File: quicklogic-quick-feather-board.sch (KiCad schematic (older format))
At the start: 48 parts, among them IC1 EOS-S3, J5 0473460001, Q1 BSS138AKA, Q2 BSS84, U1 TPS62821DLCR, U2 MCP73831T-2ACI_OT, U3 GD25Q16CWIGR, U4 DPS310, U5 MC3635, X1 ECS-_327-12_5-34B-TR

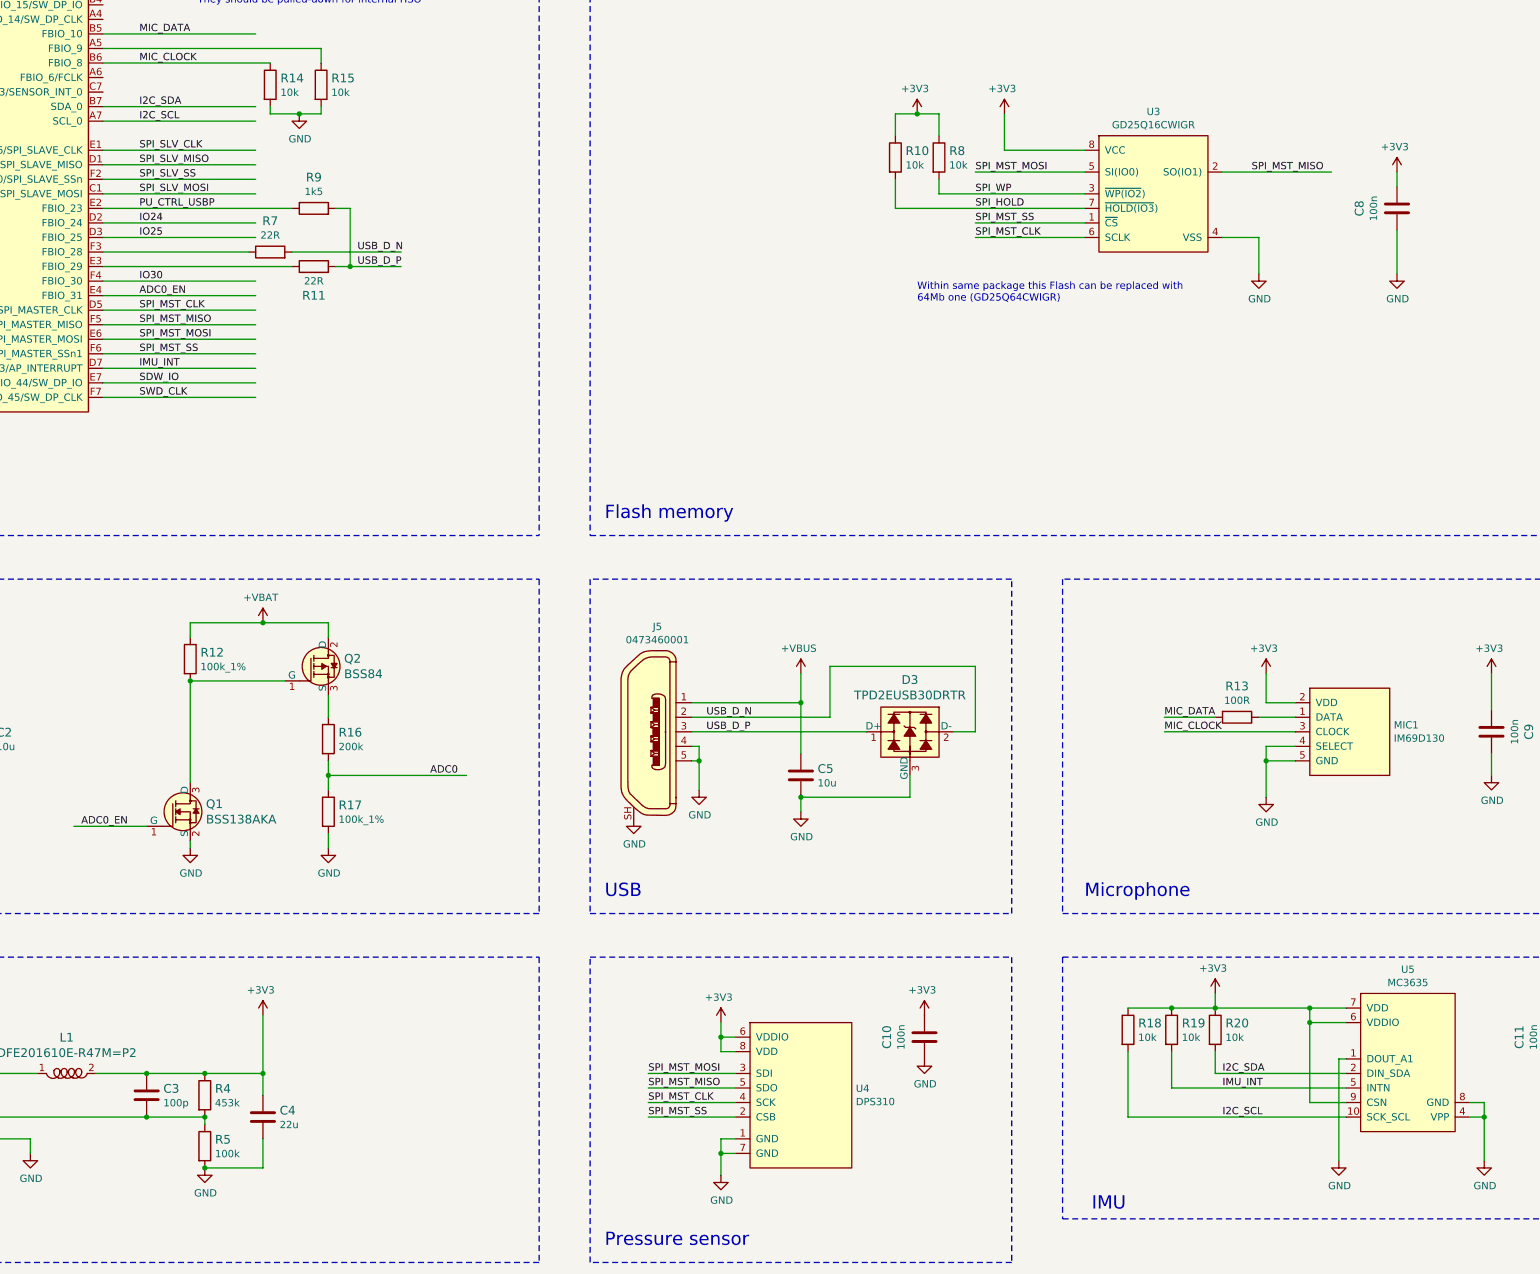
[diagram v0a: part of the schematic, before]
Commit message: Added bootstrap resistors, connected pressure sensor to I2C bus, placed components on PCB
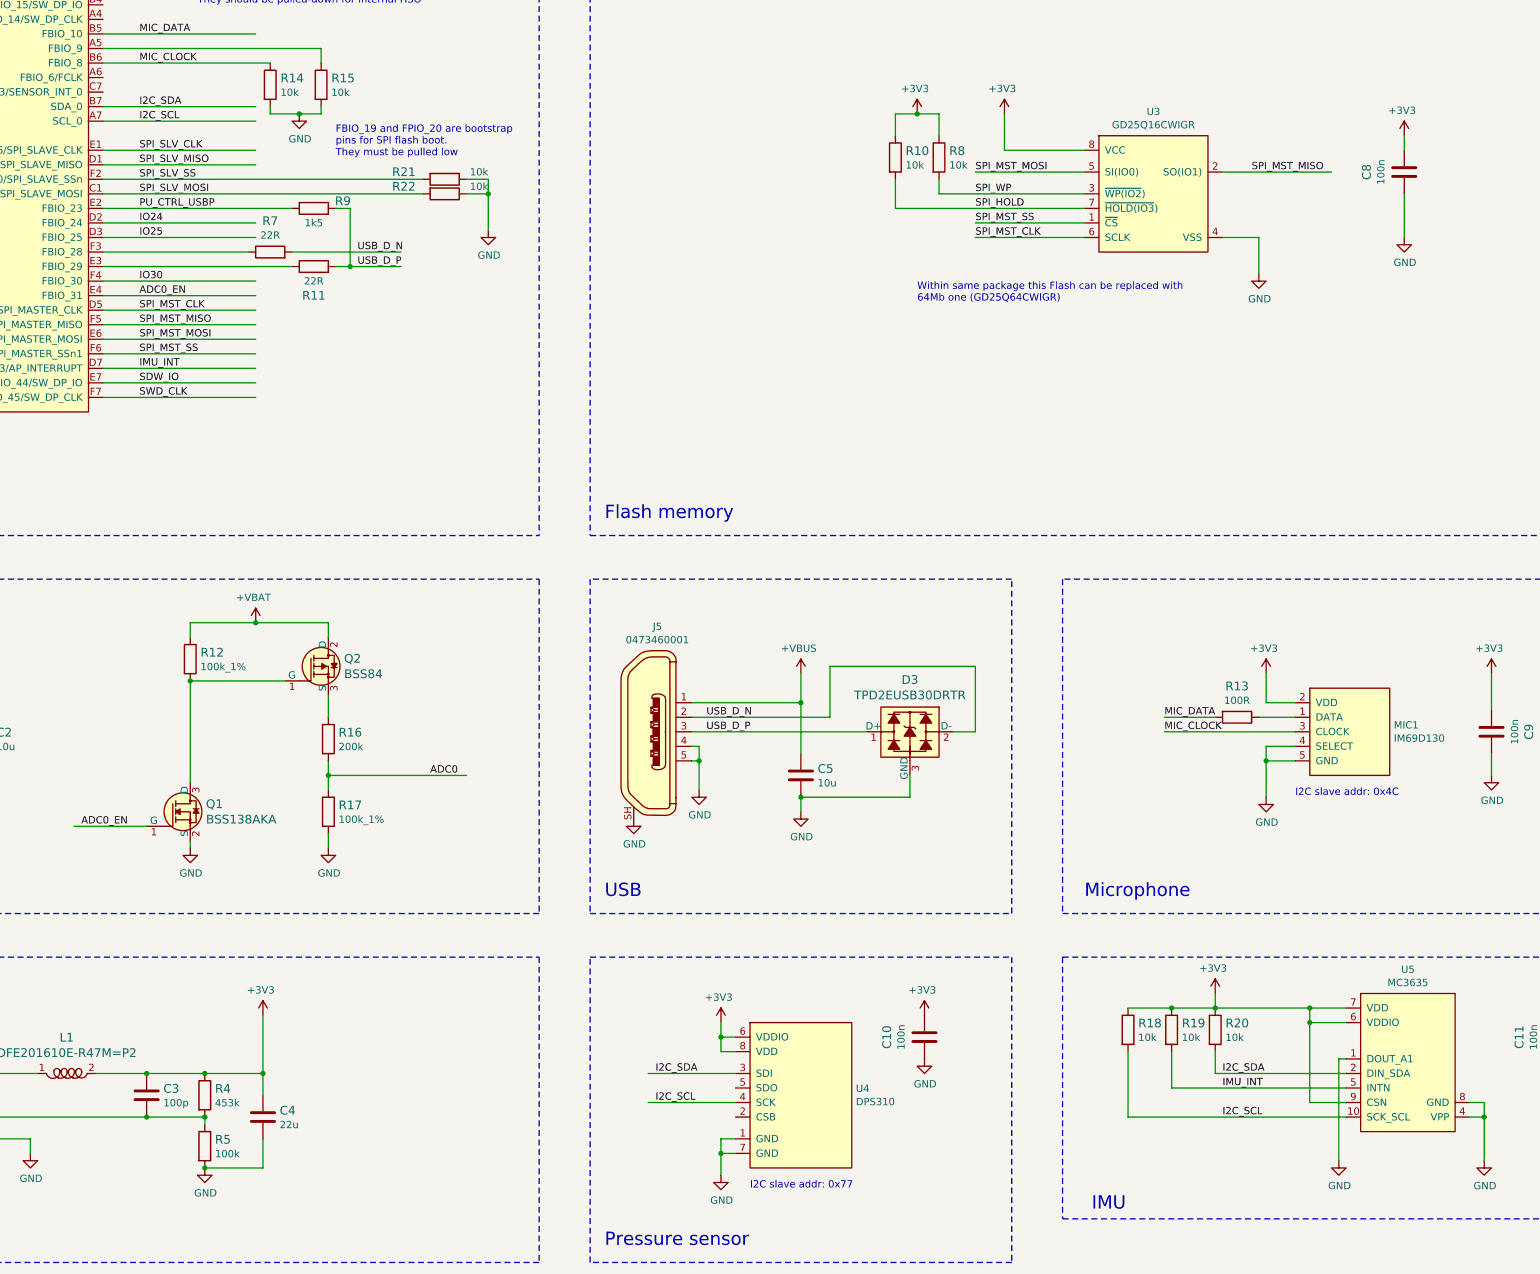
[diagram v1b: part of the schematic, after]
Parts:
- added R21, R22: R_10k_0402, quicklogic-quick-feather-board-footprints:0402-res, symbol quicklogic-quick-feather-board:R_10k_0402
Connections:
- wire segments 196 -> 198
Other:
- note added: "FBIO_19 and FPIO_20 are bootstrap\npins for SPI flash boot.\nThey must be pulled low"
- note added: "I2C slave addr: 0x4C"
- note added: "I2C slave addr: 0x77"
- moved on the sheet: C8
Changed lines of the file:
@@
 	5250 3150 6300 3150
-Wire Wire Line
-	5250 2850 6300 2850
-Wire Wire Line
-	5250 2750 6300 2750
 Wire Wire Line
 	5250 2650 6300 2650
@@
 L quicklogic-quick-feather-board:C_100n_0402_6V3 C8
 U 1 1 5DDB4C4D
-P 14150 2950
-F 0 "C8" V 13892 2950 60  0000 C CNN
-F 1 "C_100n_0402_6V3" H 14150 2800 60  0001 C CNN
-F 2 "quicklogic-quick-feather-board-footprints:0402-cap" H 14350 3150 60  0001 L CNN
-F 3 "" H 14150 2950 50  0001 C CNN
-F 4 "Walsin" H 14350 3350 60  0001 L CNN "Manufacturer"
-F 5 "0402X104K6R3CT" H 14350 3250 60  0001 L CNN "MPN"
-F 6 "100n" V 13990 2950 50  0000 C CNN "Val"
-	1    14150 2950
+P 14200 2700
+F 0 "C8" V 13942 2700 60  0000 C CNN
+F 1 "C_100n_0402_6V3" H 14200 2550 60  0001 C CNN
+F 2 "quicklogic-quick-feather-board-footprints:0402-cap" H 14400 2900 60  0001 L CNN
+F 3 "" H 14200 2700 50  0001 C CNN
+F 4 "Walsin" H 14400 3100 60  0001 L CNN "Manufacturer"
+F 5 "0402X104K6R3CT" H 14400 3000 60  0001 L CNN "MPN"
+F 6 "100n" V 14040 2700 50  0000 C CNN "Val"
+	1    14200 2700
 	1    0    0    -1
 $EndComp
@@
 Wire Wire Line
 	4150 6150 4150 6550
-Connection ~ 2750 6150
 Wire Wire Line
 	5550 9200 5950 9200
@@
 U 1 1 5DE457DE
 P 6700 2950
-F 0 "R9" H 6700 3163 60  0000 C CNN
+F 0 "R9" H 6900 3000 60  0000 C CNN
 F 1 "R_1k5_0402" H 6700 2800 60  0001 C CNN
 F 2 "quicklogic-quick-feather-board-footprints:0402-res" H 6900 3150 60  0001 L CNN
@@
 F 4 "PANASONIC_ELECTRONIC_COMPONENTS" H 6900 3350 60  0001 L CNN "Manufacturer"
 F 5 "ERJ2RKF1501X" H 6900 3250 60  0001 L CNN "MPN"
-F 6 "1k5" H 6700 3065 50  0000 C CNN "Val"
+F 6 "1k5" H 6700 2850 50  0000 C CNN "Val"
 	1    6700 2950
 	1    0    0    -1
@@
 L quicklogic-quick-feather-board:+3V3 #PWR0114
 U 1 1 5DE34948
-P 14150 2650
-F 0 "#PWR0114" H 14150 2650 50  0001 C CNN
-F 1 "+3V3" H 14135 2773 50  0000 C CNN
-F 2 "" H 14150 2650 50  0001 C CNN
-F 3 "" H 14150 2650 50  0001 C CNN
-	1    14150 2650
+P 14200 2400
+F 0 "#PWR0114" H 14200 2400 50  0001 C CNN
+F 1 "+3V3" H 14185 2523 50  0000 C CNN
+F 2 "" H 14200 2400 50  0001 C CNN
+F 3 "" H 14200 2400 50  0001 C CNN
+	1    14200 2400
 	1    0    0    -1
 $EndComp
@@
 	13200 3150 13200 3400
 Wire Wire Line
-	14150 3100 14150 3400
+	14200 2850 14200 3150
 $Comp
 L quicklogic-quick-feather-board:GND #PWR0115
 U 1 1 5DE3FA98
-P 14150 3400
-F 0 "#PWR0115" H 14150 3150 50  0001 C CNN
-F 1 "GND" H 14155 3227 50  0000 C CNN
-F 2 "" H 14150 3400 50  0001 C CNN
-F 3 "" H 14150 3400 50  0001 C CNN
-	1    14150 3400
-	1    0    0    -1
-$EndComp
-Wire Wire Line
-	14150 2700 14150 2800
+P 14200 3150
+F 0 "#PWR0115" H 14200 2900 50  0001 C CNN
+F 1 "GND" H 14205 2977 50  0000 C CNN
+F 2 "" H 14200 3150 50  0001 C CNN
+F 3 "" H 14200 3150 50  0001 C CNN
+	1    14200 3150
+	1    0    0    -1
+$EndComp
+Wire Wire Line
+	14200 2450 14200 2550
 $Comp
 L quicklogic-quick-feather-board:+3V3 #PWR0116
@@
 $EndComp
 Connection ~ 6350 8900
-$Comp
-L quicklogic-quick-feather-board:+VBUS #PWR0119
-U 1 1 5DE69BB0
-P 2750 6100
-F 0 "#PWR0119" H 2750 6100 50  0001 C CNN
-F 1 "+VBUS" H 2735 6223 50  0000 C CNN
-F 2 "" H 2750 6100 50  0001 C CNN
-F 3 "" H 2750 6100 50  0001 C CNN
-	1    2750 6100
-	1    0    0    -1
-$EndComp
-$Comp
-L quicklogic-quick-feather-board:+VBAT #PWR0120
-U 1 1 5DE6A679
-P 4400 6400
-F 0 "#PWR0120" H 4400 6400 50  0001 C CNN
-F 1 "+VBAT" H 4385 6523 50  0000 C CNN
-F 2 "" H 4400 6400 50  0001 C CNN
-F 3 "" H 4400 6400 50  0001 C CNN
-	1    4400 6400
-	1    0    0    -1
-$EndComp
-Connection ~ 4400 6450
-$Comp
-L quicklogic-quick-feather-board:+VBAT #PWR0121
-U 1 1 5DE6ABAC
-P 2450 8450
-F 0 "#PWR0121" H 2450 8450 50  0001 C CNN
-F 1 "+VBAT" H 2435 8573 50  0000 C CNN
-F 2 "" H 2450 8450 50  0001 C CNN
-F 3 "" H 2450 8450 50  0001 C CNN
-	1    2450 8450
-	1    0    0    -1
-$EndComp
-$Comp
-L quicklogic-quick-feather-board:+VBUS #PWR0122
-U 1 1 5DE6B20E
-P 1950 8450
-F 0 "#PWR0122" H 1950 8450 50  0001 C CNN
-F 1 "+VBUS" H 1935 8573 50  0000 C CNN
-F 2 "" H 1950 8450 50  0001 C CNN
-F 3 "" H 1950 8450 50  0001 C CNN
-	1    1950 8450
-	1    0    0    -1
-$EndComp
 Wire Wire Line
 	1950 8900 1950 8500
 Wire Wire Line
 	6350 8500 6350 8900
-$Comp
-L quicklogic-quick-feather-board:+VBUS #PWR0123
-U 1 1 5DE7906C
-P 10050 6100
-F 0 "#PWR0123" H 10050 6100 50  0001 C CNN
-F 1 "+VBUS" H 10035 6223 50  0000 C CNN
-F 2 "" H 10050 6100 50  0001 C CNN
-F 3 "" H 10050 6100 50  0001 C CNN
-	1    10050 6100
-	1    0    0    -1
-$EndComp
 Wire Wire Line
 	10050 6150 10050 6350
@@
 Wire Wire Line
 	9500 9450 9500 9600
-Text Label 9000 8900 0    50   ~ 0
-SPI_MST_MOSI
-Text Label 9000 9000 0    50   ~ 0
-SPI_MST_MISO
-Text Label 9000 9100 0    50   ~ 0
-SPI_MST_CLK
-Text Label 9000 9200 0    50   ~ 0
-SPI_MST_SS
 Wire Wire Line
 	9600 8900 9000 8900
-Wire Wire Line
-	9600 9000 9000 9000
-Wire Wire Line
-	9600 9100 9000 9100
-Wire Wire Line
-	9600 9200 9000 9200
 Wire Notes Line
 	8600 8100 11500 8100
@@
 $EndComp
 Connection ~ 5850 6200
-$Comp
-L quicklogic-quick-feather-board:+VBAT #PWR0126
-U 1 1 5DE26AAF
-P 6350 5750
-F 0 "#PWR0126" H 6350 5750 50  0001 C CNN
-F 1 "+VBAT" H 6335 5873 50  0000 C CNN
-F 2 "" H 6350 5750 50  0001 C CNN
-F 3 "" H 6350 5750 50  0001 C CNN
-	1    6350 5750
-	1    0    0    -1
-$EndComp
-Wire Wire Line
-	6350 5800 5850 5800
 Wire Wire Line
 	5850 5800 5850 5900
 Wire Wire Line
-	6350 5800 6800 5800
-Wire Wire Line
 	6800 5800 6800 5900
-Connection ~ 6350 5800
 Text Notes 5900 1550 0    50   ~ 0
 FBIO_8 and FBIO_9 are bootstrap pins for HS oscillator.\nThey should be pulled-down for internal HSO
@@
 Text Label 5500 3550 0    50   ~ 0
 ADC0_EN
+$Comp
+L quicklogic-quick-feather-board:R_10k_0402 R21
+U 1 1 5DF80444
+P 7600 2750
+F 0 "R21" H 7800 2700 60  0000 L CNN
+F 1 "R_10k_0402" H 7600 2600 60  0001 C CNN
+F 2 "quicklogic-quick-feather-board-footprints:0402-res" H 7800 2950 60  0001 L CNN
+F 3 "" H 7600 2750 50  0001 C CNN
+F 4 "VISHAY" H 7800 3150 60  0001 L CNN "Manufacturer"
+F 5 "CRCW040210K0FKEDHP" H 7800 3050 60  0001 L CNN "MPN"
+F 6 "10k" H 7300 2700 50  0000 L CNN "Val"
+	1    7600 2750
+	-1   0    0    1
+$EndComp
+$Comp
+L quicklogic-quick-feather-board:R_10k_0402 R22
+U 1 1 5DF80FDB
+P 7600 2850
+F 0 "R22" H 7800 2800 60  0000 L CNN
+F 1 "R_10k_0402" H 7600 2700 60  0001 C CNN
+F 2 "quicklogic-quick-feather-board-footprints:0402-res" H 7800 3050 60  0001 L CNN
+F 3 "" H 7600 2850 50  0001 C CNN
+F 4 "VISHAY" H 7800 3250 60  0001 L CNN "Manufacturer"
+F 5 "CRCW040210K0FKEDHP" H 7800 3150 60  0001 L CNN "MPN"
+F 6 "10k" H 7300 2800 50  0000 L CNN "Val"
+	1    7600 2850
+	-1   0    0    1
+$EndComp
+Wire Wire Line
+	5250 2750 7450 2750
+Wire Wire Line
+	5250 2850 7450 2850
+Wire Wire Line
+	7750 2750 7900 2750
+Wire Wire Line
+	7900 2750 7900 2850
+Wire Wire Line
+	7750 2850 7900 2850
+Connection ~ 7900 2850
+Wire Wire Line
+	7900 2850 7900 3100
+$Comp
+L quicklogic-quick-feather-board:GND #PWR0133
+U 1 1 5DFB6470
+P 7900 3100
+F 0 "#PWR0133" H 7900 2850 50  0001 C CNN
+F 1 "GND" H 7905 2927 50  0000 C CNN
+F 2 "" H 7900 3100 50  0001 C CNN
+F 3 "" H 7900 3100 50  0001 C CNN
+	1    7900 3100
+	1    0    0    -1
+$EndComp
+Text Notes 6850 2600 0    50   ~ 0
+FBIO_19 and FPIO_20 are bootstrap\npins for SPI flash boot.\nThey must be pulled low
+Wire Wire Line
+	9600 9100 9000 9100
+Text Notes 13450 7000 0    50   ~ 0
+I2C slave addr: 0x4C
+Text Notes 9700 9700 0    50   ~ 0
+I2C slave addr: 0x77
+Text Label 9050 9100 0    50   ~ 0
+I2C_SCL
+Text Label 9050 8900 0    50   ~ 0
+I2C_SDA
+$Comp
+L quicklogic-quick-feather-board:+VBUS #PWR0119
+U 1 1 5E01B939
+P 2750 6100
+F 0 "#PWR0119" H 2750 6100 50  0001 C CNN
+F 1 "+VBUS" H 2735 6223 50  0000 C CNN
+F 2 "" H 2750 6100 50  0001 C CNN
+F 3 "" H 2750 6100 50  0001 C CNN
+	1    2750 6100
+	1    0    0    -1
+$EndComp
+Connection ~ 2750 6150
+$Comp
+L quicklogic-quick-feather-board:+VBUS #PWR0120
+U 1 1 5E01C077
+P 10050 6100
+F 0 "#PWR0120" H 10050 6100 50  0001 C CNN
+F 1 "+VBUS" H 10035 6223 50  0000 C CNN
+F 2 "" H 10050 6100 50  0001 C CNN
+F 3 "" H 10050 6100 50  0001 C CNN
+	1    10050 6100
+	1    0    0    -1
+$EndComp
+$Comp
+L quicklogic-quick-feather-board:+VBAT #PWR0122
+U 1 1 5E029586
+P 6300 5750
+F 0 "#PWR0122" H 6300 5750 50  0001 C CNN
+F 1 "+VBAT" H 6285 5873 50  0000 C CNN
+F 2 "" H 6300 5750 50  0001 C CNN
+F 3 "" H 6300 5750 50  0001 C CNN
+	1    6300 5750
+	1    0    0    -1
+$EndComp
+Wire Wire Line
+	5850 5800 6300 5800
+Connection ~ 6300 5800
+Wire Wire Line
+	6300 5800 6800 5800
+$Comp
+L quicklogic-quick-feather-board:+VBUS #PWR0123
+U 1 1 5E029AF7
+P 1950 8450
+F 0 "#PWR0123" H 1950 8450 50  0001 C CNN
+F 1 "+VBUS" H 1935 8573 50  0000 C CNN
+F 2 "" H 1950 8450 50  0001 C CNN
+F 3 "" H 1950 8450 50  0001 C CNN
+	1    1950 8450
+	1    0    0    -1
+$EndComp
+$Comp
+L quicklogic-quick-feather-board:+VBAT #PWR0126
+U 1 1 5E02A13E
+P 2450 8450
+F 0 "#PWR0126" H 2450 8450 50  0001 C CNN
+F 1 "+VBAT" H 2435 8573 50  0000 C CNN
+F 2 "" H 2450 8450 50  0001 C CNN
+F 3 "" H 2450 8450 50  0001 C CNN
+	1    2450 8450
+	1    0    0    -1
+$EndComp
+$Comp
+L quicklogic-quick-feather-board:+VBAT #PWR?
+U 1 1 5E035BA1
+P 4400 6400
+F 0 "#PWR?" H 4400 6400 50  0001 C CNN
+F 1 "+VBAT" H 4385 6523 50  0000 C CNN
+F 2 "" H 4400 6400 50  0001 C CNN
+F 3 "" H 4400 6400 50  0001 C CNN
+	1    4400 6400
+	1    0    0    -1
+$EndComp
+Connection ~ 4400 6450
 $EndSCHEMATC
